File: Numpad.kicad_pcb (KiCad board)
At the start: 2 copper layers, 76.2 x 95 mm, 55 parts, among them J1 USB_B_Mini, SW0 0, SW1 1, SW2 2, SW3 3, SW4 4, SW5 5, SW6 6, SW7 7, SW8 8, SW9 9, U1 ATmega32U4-AU, Y1 16MHz

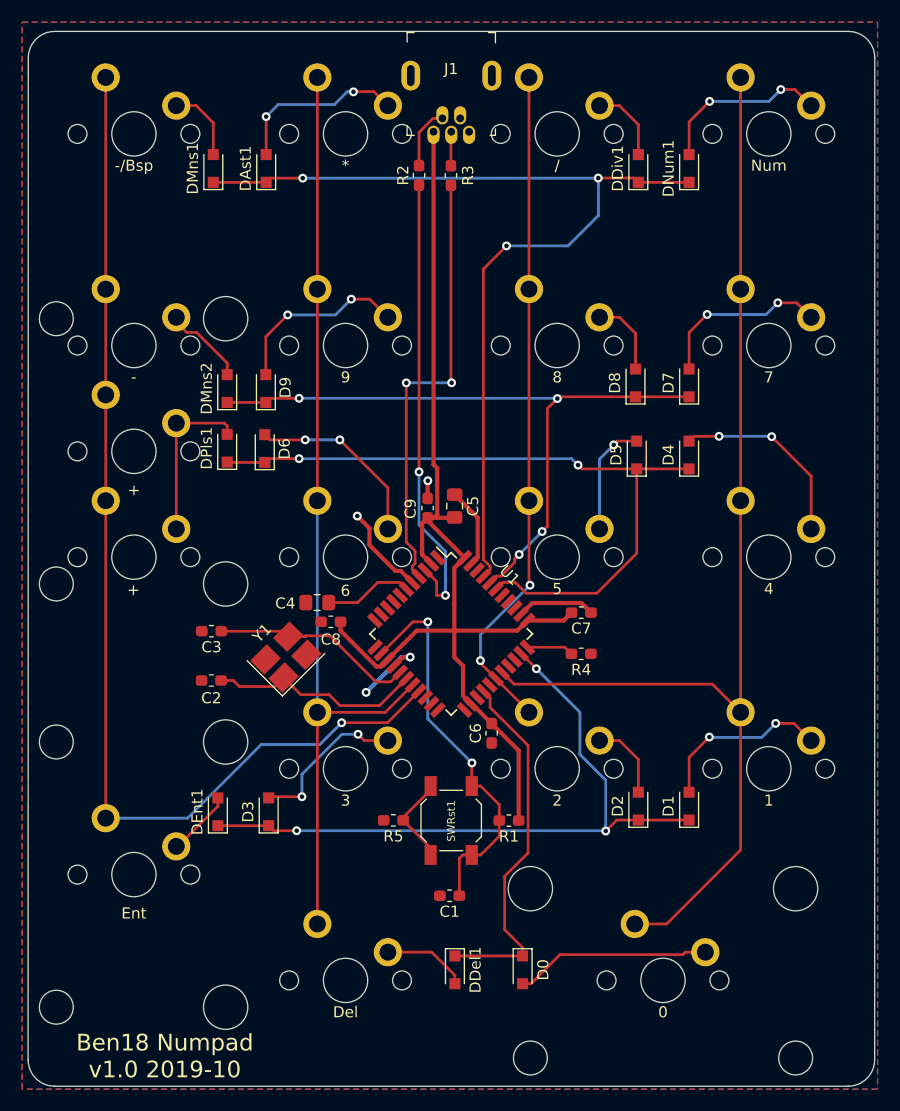
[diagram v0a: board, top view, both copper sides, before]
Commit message: Rotated Pls & Rtn switches, they are loose in the plate in original orientation
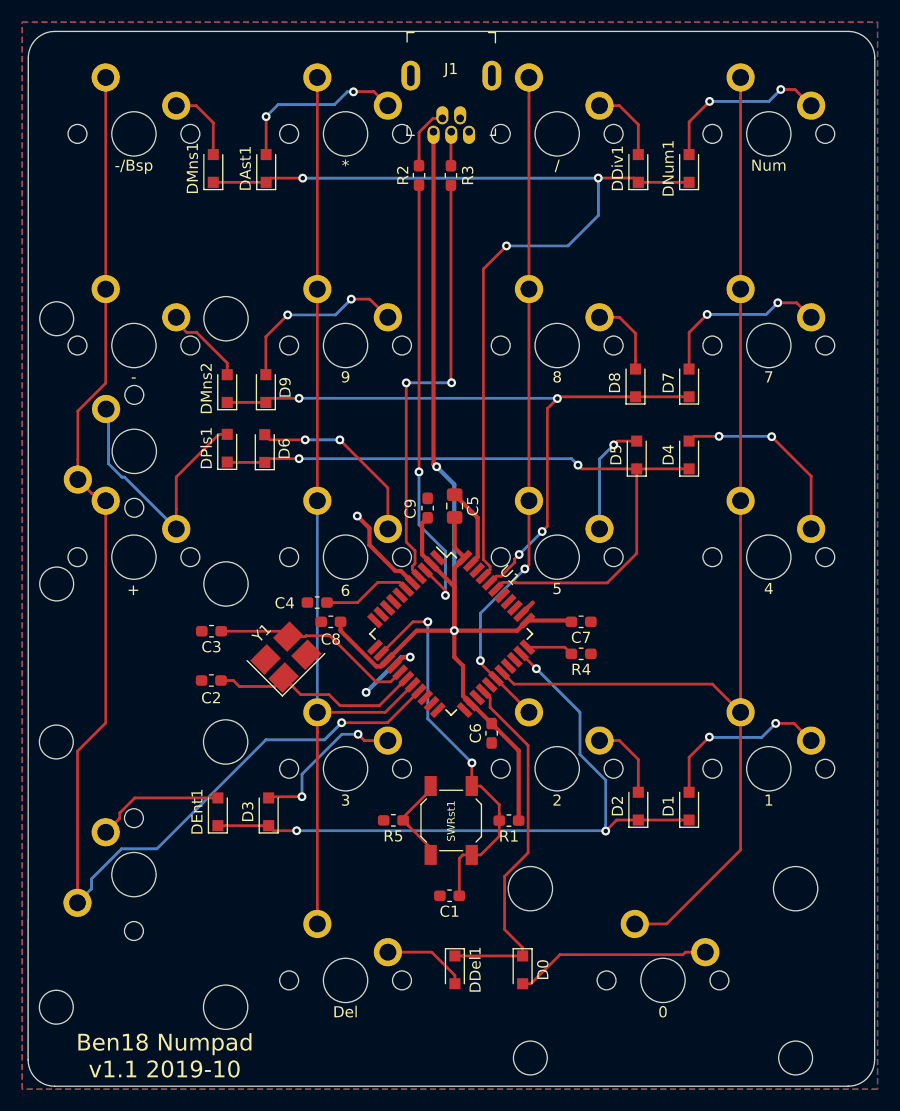
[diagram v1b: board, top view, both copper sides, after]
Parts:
- C4: footprint Capacitor_SMD:C_0805_2012Metric_Pad1.15x1.40mm_HandSolder -> Capacitor_SMD:C_0603_1608Metric_Pad1.05x0.95mm_HandSolder
- SWEnt1, SWPls1: footprint AcheronMX:MX200VR -> AcheronMX:MX200
- moved C7 0.83 mm to (159.8, 105.6)
- turned SWPls1 to 90 degrees
- turned SWEnt1 to 90 degrees
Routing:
- net Col4: track 99.6 -> 116.9 mm
- net +5V: track 100.4 -> 114.0 mm, vias 0 -> 2
- net Net-(DPls1-Pad2): track 15.0 -> 24.4 mm
- net GND: track 31.5 -> 24.3 mm, vias 4 -> 3
- net Net-(DEnt1-Pad2): track 5.99 -> 11.7 mm
- net Row3: track 65.1 -> 64.3 mm
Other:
- board text added: "Ben18 Numpad v1.1 2019-10"
- board text removed: "Ben18 Numpad v1.0 2019-10"

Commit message: I hadnt connected the VBUS, changed it back to 17 keys no option for split plus.
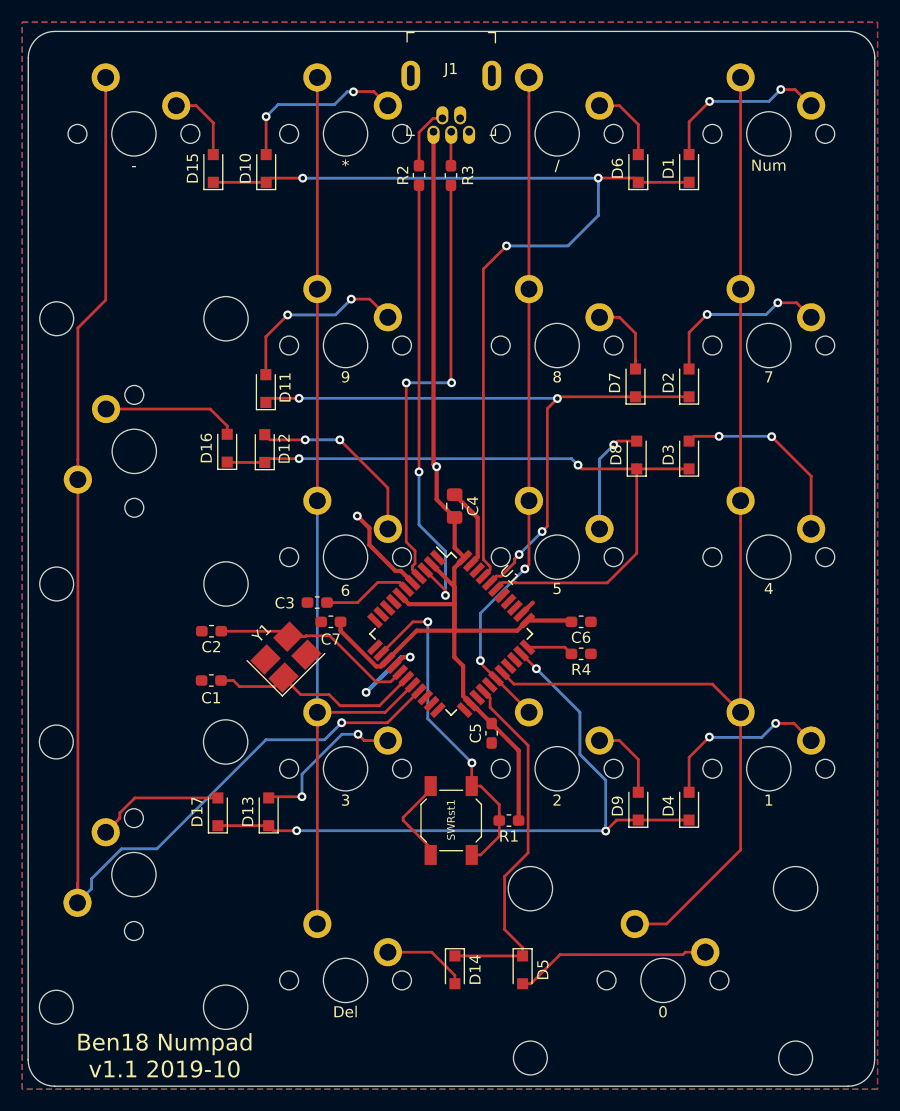
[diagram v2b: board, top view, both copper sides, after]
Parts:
- removed the C1 at (148.0, 130.2)
- removed C9: 0.1uF, Capacitor_SMD:C_0603_1608Metric_Pad1.05x0.95mm_HandSolder
- removed DMns2: 1N4148W, Diode_SMD:D_SOD-323_HandSoldering
- removed R5: 330, Resistor_SMD:R_0603_1608Metric_Pad1.05x0.95mm_HandSolder
- removed SWMns2: -, AcheronMX:MX100
- removed SWPls2: +, AcheronMX:MX100
- C4: renamed from C5; value 4.7uF -> 10uF
- SW15: renamed from SWMns1; value -/Bsp -> -
- turned SWRst1 to 90 degrees
- renumbered C2 to C1, C3 to C2, C4 to C3, C6 to C5, C7 to C6, C8 to C7, DNum1 to D1, DAst1 to D10, D9 to D11, D6 to D12, D3 to D13, DDel1 to D14, DMns1 to D15, DPls1 to D16, DEnt1 to D17, D7 to D2, D4 to D3, D1 to D4, D0 to D5, DDiv1 to D6, D8 to D7, D5 to D8, D2 to D9, SWNum1 to SW1, SWAst1 to SW10, SW9 to SW11, SW6 to SW12, SW3 to SW13, SWDel1 to SW14, SWPls1 to SW16, SWEnt1 to SW17, SW7 to SW2, SW4 to SW3, SW1 to SW4, SW0 to SW5, SWDiv1 to SW6, SW8 to SW7, SW5 to SW8, SW2 to SW9
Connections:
- SWRst1 pad 1: RST -> GND
- SWRst1 pad 2: Net-(R5-Pad1) -> RST
- U1 pad 7: Net-(U1-Pad7) -> +5V
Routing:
- net Net-(D16-Pad2): track 24.4 -> 12.6 mm
- net +5V: track 114.0 -> 103.9 mm, vias 2 -> 1
- net Net-(R5-Pad1): track 8.25 -> 0.00 mm
- net GND: track 24.3 -> 32.5 mm
- net Net-(DMns2-Pad2): track 7.58 -> 0.00 mm
- net RST: track 35.6 -> 31.0 mm
- net Row2: track 61.2 -> 57.7 mm
- net Col4: track 116.9 -> 116.3 mm
